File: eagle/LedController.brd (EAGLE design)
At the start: 64.8 x 34.3 mm, 32 parts, among them IC1 MCP601R, Q1 16MHz, Q5 PMV20EN, X1 2510-, X2 MKDSN1,5/4-5,08

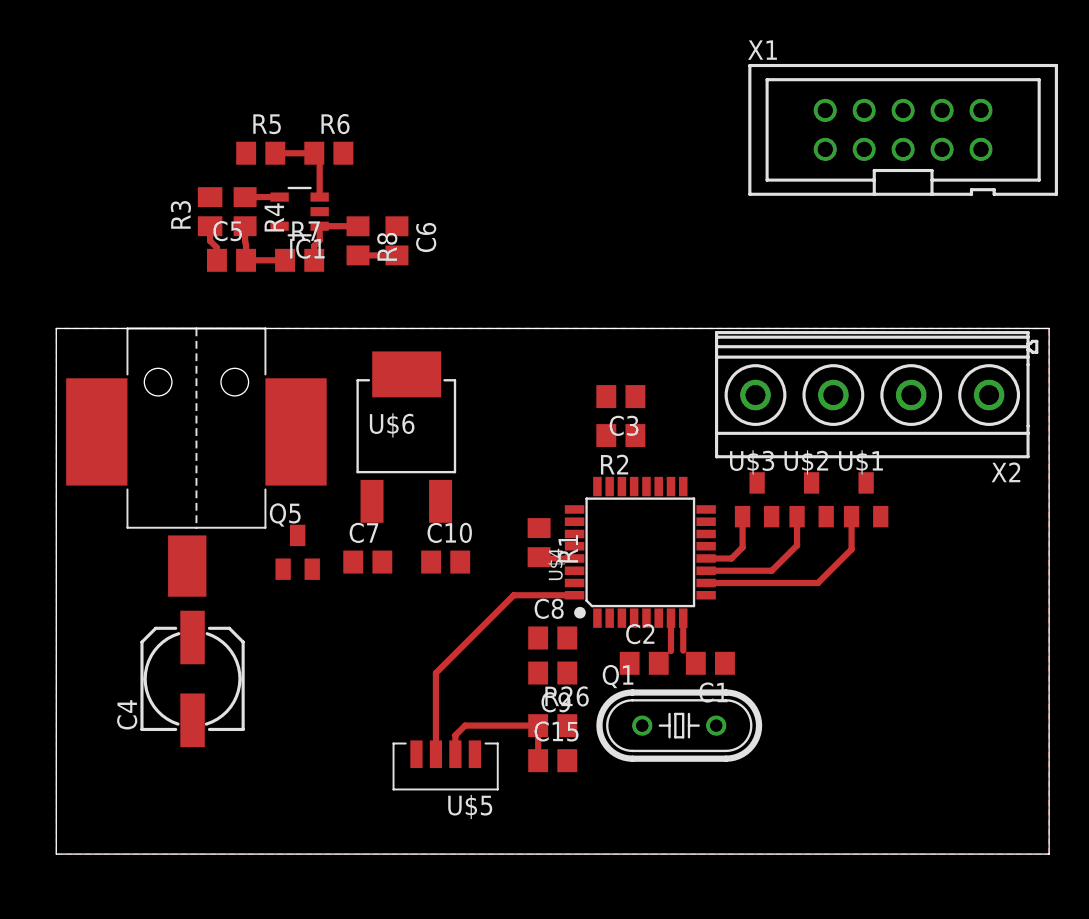
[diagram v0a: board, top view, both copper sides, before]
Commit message: Change crystal to SMD type
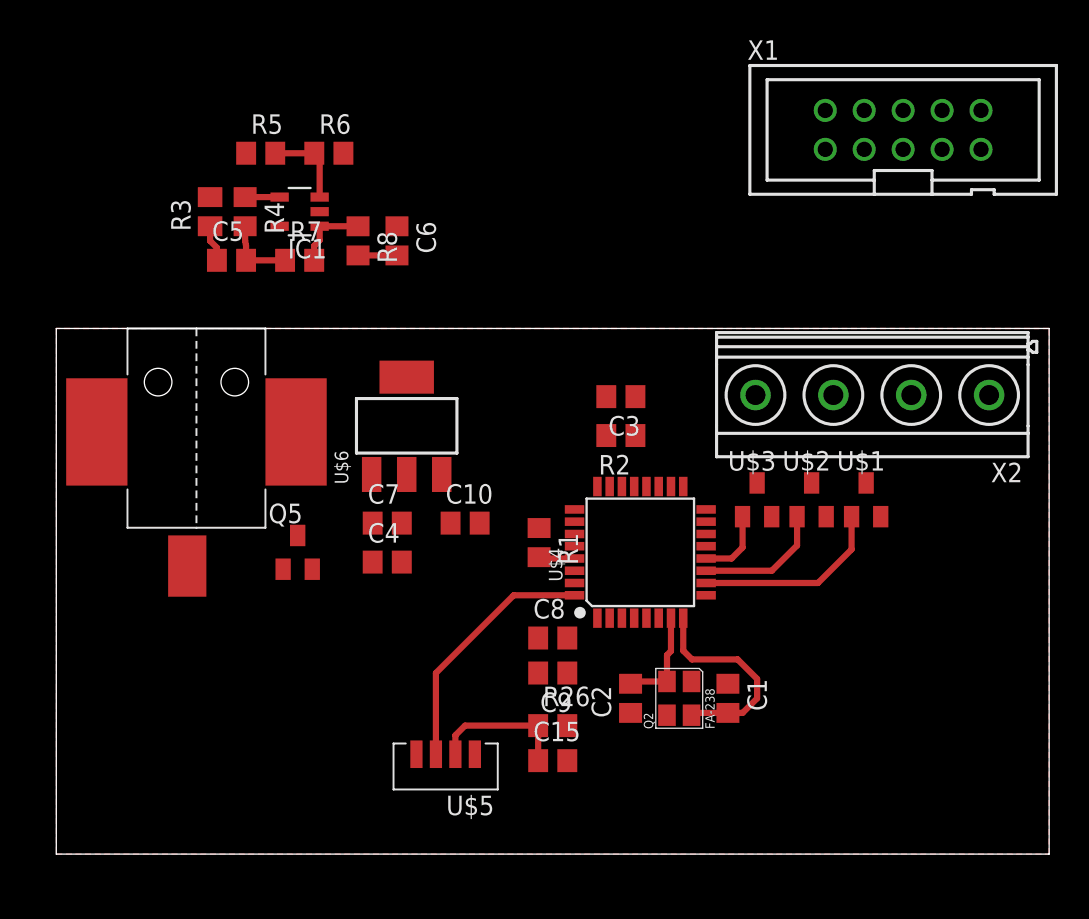
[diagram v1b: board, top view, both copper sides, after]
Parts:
- removed Q1: 16MHz, crystal:HC49/S
- added Q2: FA-238, LedController:FA-238
- C4: value 100uF -> 10uF; device rcl:153CLV-0605 -> rcl:C0805
- U$6: value L78M05ABDT-TR -> UA78M05; device LedController:DPAK -> LedController:SOT-223
- moved C4 14.8 mm to (21.6, 19.1), turned to 0 degrees
- moved C10 2.84 mm to (26.7, 21.6)
- moved C7 2.84 mm to (21.6, 21.6)
- moved C1 2.56 mm to (43.8, 10.2), turned to 270 degrees
- moved C2 2.45 mm to (37.5, 10.2), turned to 90 degrees
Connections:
- removed net N$2: C1.2, Q1.2
- net +12V: now also C4.1; no longer C4.+
- net GND: now also C4.2, Q2.2, Q2.4, U$6.2, U$6.TER; no longer C4.-, U$6.4
- net N$13: now also C1.2, Q2.1
- net N$14: now also Q2.3; no longer Q1.1
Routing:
- net N$13: track 2.12 -> 13.7 mm
- net N$14: track 2.15 -> 6.77 mm

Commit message: Change ISP Connector, layout most things
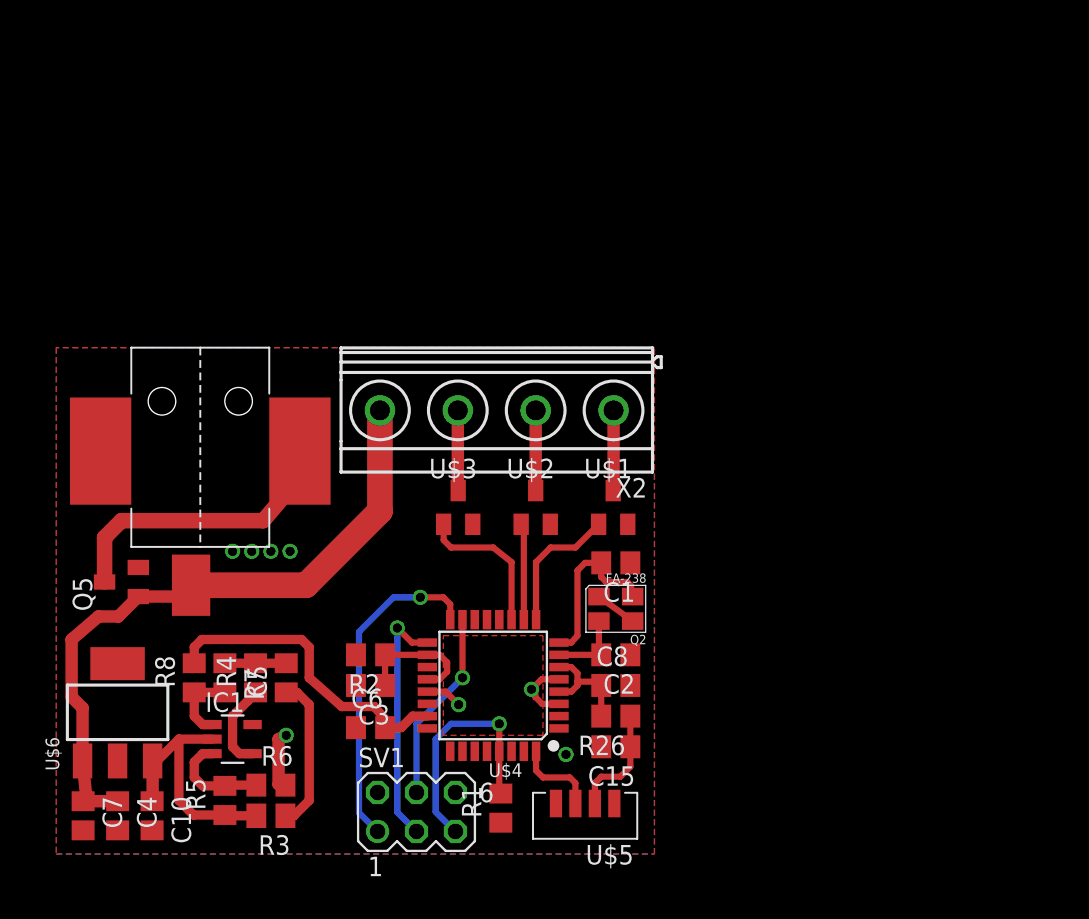
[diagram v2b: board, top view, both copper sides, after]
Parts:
- removed C9: 100nF, rcl:C0805
- removed X1: 2510-, con-3m:PAK100/2500-10
- added SV1: ISP, con-lstb:MA03-2
- moved R5 42.3 mm to (11.0, 3.50), turned to 90 degrees
- moved R6 41.4 mm to (14.0, 4.50)
- moved R3 39.6 mm to (14.0, 2.50), turned to 180 degrees
- moved IC1 34.7 mm to (11.5, 7.50), turned to 270 degrees
- moved C6 31.8 mm to (20.5, 8.25), turned to 0 degrees
- moved R8 30.4 mm to (9.00, 11.5), turned to 90 degrees
- moved R4 30.4 mm to (13.0, 11.5), turned to 90 degrees
- moved C10 28.0 mm to (6.25, 2.50), turned to 270 degrees
- moved R7 27.7 mm to (11.0, 11.5), turned to 270 degrees
- moved C7 27.5 mm to (1.75, 2.50), turned to 270 degrees
- moved C5 27.5 mm to (15.0, 11.5), turned to 90 degrees
- moved U$6 26.6 mm to (4.00, 9.25)
- moved C3 24.9 mm to (20.5, 11.0)
- moved X2 24.5 mm to (28.7, 29.0)
- moved C4 24.2 mm to (4.00, 2.50), turned to 270 degrees
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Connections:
- net +5V: now also C8.1, SV1.2; no longer X1.2
- net GND: now also C8.2, SV1.6; no longer X1.10, X1.4, X1.6, X1.8
- net ISP_CLK: now also SV1.3; no longer X1.7
- net ISP_MISO: now also SV1.1; no longer X1.9
- net ISP_MOSI: now also SV1.4; no longer X1.1
- net ISP_RESET: now also SV1.5; no longer X1.5
- net PWM_B: now also U$4.11; no longer U$4.12
- net PWM_G: now also U$4.10; no longer U$4.11
- net PWM_R: now also U$4.9; no longer U$4.10
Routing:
- net +12V: track 0.00 -> 45.5 mm
- net +5V: track 0.00 -> 25.5 mm
- net ISP_MISO: track 0.00 -> 21.6 mm, vias 0 -> 1
- net N$8: track 0.00 -> 18.9 mm
- net ADC: track 2.54 -> 20.6 mm
- net ISP_CLK: track 0.00 -> 16.1 mm, vias 0 -> 1
- net GND: track 0.00 -> 13.5 mm, vias 0 -> 8
- net ISP_RESET: track 2.35 -> 15.7 mm, vias 0 -> 1
- net ISP_MOSI: track 0.00 -> 12.5 mm, vias 0 -> 1
- net IR: track 16.4 -> 5.49 mm
- net N$7: track 0.00 -> 8.36 mm
- net N$1: track 2.41 -> 10.0 mm
- net N$6: track 0.00 -> 5.23 mm
- net N$4: track 0.00 -> 5.23 mm
- net N$5: track 0.00 -> 5.23 mm
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- added copper zone on layer 16, net GND
- added copper zone on layer 1, net N$2
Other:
- board outline removed

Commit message: More relayouting, Framed schematic
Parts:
- moved C4 15.5 mm to (3.00, 18.0), turned to 180 degrees
- moved C7 13.6 mm to (3.00, 16.0), turned to 180 degrees
- moved R3 12.5 mm to (1.50, 2.50), turned to 90 degrees
- moved R8 11.9 mm to (20.0, 7.00), turned to 0 degrees
- moved Q5 11.7 mm to (15.8, 20.0), turned to 0 degrees
- moved R7 11.4 mm to (16.5, 1.50), turned to 0 degrees
- moved C5 11.0 mm to (10.5, 1.50), turned to 0 degrees
- moved R4 9.01 mm to (13.5, 2.50), turned to 270 degrees
- moved C10 5.55 mm to (3.00, 7.00), turned to 180 degrees
- moved R6 3.64 mm to (10.5, 3.50), turned to 180 degrees
- moved IC1 3.09 mm to (14.5, 6.75), turned to 180 degrees
- moved U$6 2.70 mm to (5.50, 11.5), turned to 270 degrees
- moved R5 2.06 mm to (10.5, 5.50), turned to 0 degrees
- moved C6 0.90 mm to (20.0, 9.00)
- moved SV1 0.75 mm to (22.8, 2.75)
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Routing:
- net +5V: track 25.5 -> 81.6 mm, vias 0 -> 3
- net ADC: track 20.6 -> 5.46 mm
- net N$8: track 18.9 -> 5.59 mm
- net ISP_RESET: track 15.7 -> 7.86 mm, vias 1 -> 0
- net N$12: track 4.97 -> 10.0 mm
- net +12V: track 45.5 -> 40.8 mm
- net ISP_MISO: track 21.6 -> 17.2 mm
- net N$10: track 5.65 -> 2.00 mm
- net N$1: track 10.0 -> 8.07 mm
- net ISP_MOSI: track 12.5 -> 14.3 mm
- net N$11: track 7.60 -> 6.30 mm
- net GND: track 13.5 -> 12.5 mm, vias 8 -> 18
- net N$9: track 4.00 -> 4.51 mm
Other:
- board outline added: 39.2 x 33.2 mm
